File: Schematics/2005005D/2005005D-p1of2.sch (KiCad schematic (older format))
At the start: 2 parts, among them J1 ConnectorB8-100, J2 ConnectorB8-200

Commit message: Finished placing components on drawing 2005005D, and added all of the wiring.  However, there's still a considerable amount of cleanup to be done.
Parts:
- added CR? (x28): Diode, symbol AGC_DSKY:Diode
- added G1: Ground-chassis, symbol AGC_DSKY:Ground-chassis
- added Q? (x56): Transistor-NPN, symbol AGC_DSKY:Transistor-NPN
- added T1, T? (x9): KCORE-PBLKCDGJ, symbol AGC_DSKY:KCORE-PBLKCDGJ
- added T21, T22, T? (x8): KCORE-PBCDKLGJ, symbol AGC_DSKY:KCORE-PBCDKLGJ
- added T23, T24: KCORE-BPCDKLGJ, symbol AGC_DSKY:KCORE-BPCDKLGJ
- added T? (x6): KCORE-BPLKCDGJ, symbol AGC_DSKY:KCORE-BPLKCDGJ
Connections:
- net at J1.110: now also Q?.1 (C), Q?.3 (E), T?.3 (C)
- net at J1.114: now also T?.1 (P)
- net at J1.116: now also T?.8 (J), T?.8 (J)
- net at J1.117: now also CR?.1 (K)
- net at J1.119: now also T?.3 (C)
- net at J1.102: now also Q?.1 (C)
- net at J1.120: now also CR?.1 (K)
- net at J1.121: now also Q?.1 (C), Q?.3 (E), T?.3 (C)
- net at J1.124: now also T?.1 (P)
- net at J1.126: now also T?.8 (J), T?.8 (J)
- net at J1.127: now also CR?.1 (K)
- net at J1.129: now also Q?.1 (C), Q?.3 (E), T?.3 (C)
- net at J1.103: now also T21.1 (P)
- net at J1.130: now also CR?.1 (K)
- net at J1.134: now also T1.1 (P)
- net at J1.136: now also T?.8 (J), T?.8 (J)
- net at J1.137: now also CR?.1 (K)
- net at J1.139: now also Q?.1 (C), Q?.3 (E), T1.3 (C)
- net at J1.104: now also Q?.3 (E), T21.4 (D)
- net at J1.140: now also CR?.1 (K)
- net at J1.141: now also Q?.1 (C), Q?.3 (E), T?.3 (C)
- net at J1.145: now also T?.1 (P)
- net at J1.147: now also T?.8 (J), T?.8 (J)
- net at J1.148: now also CR?.1 (K)
- net at J1.149: now also Q?.3 (E), T?.3 (C)
- net at J1.105: now also T21.8 (J), T22.8 (J), T23.8 (J), T24.8 (J)
- net at J1.150: now also CR?.1 (K)
- net at J1.151: now also Q?.1 (C)
- net at J1.152: now also Q?.1 (C)
- net at J1.153: now also J2.266, Q?.3 (E), Q?.3 (E), Q?.3 (E), Q?.3 (E), Q?.3 (E), Q?.3 (E), Q?.3 (E), Q?.3 (E), T?.5 (K), T?.5 (K), T?.5 (K), T?.5 (K), T?.5 (K), T?.5 (K), T?.5 (K), T?.5 (K)
- net at J1.155: now also T?.1 (P)
- net at J1.156: now also Q?.3 (E), T?.4 (D)
- net at J1.157: now also T?.8 (J), T?.8 (J), T?.8 (J), T?.8 (J)
- net at J1.158: now also CR?.1 (K)
- net at J1.106: now also CR?.1 (K)
- net at J1.160: now also CR?.1 (K)
- net at J1.161: now also Q?.3 (E), T?.4 (D)
- net at J1.163: now also Q?.1 (C)
- net at J1.164: now also T?.1 (P)
- net at J1.165: now also T?.8 (J), T?.8 (J), T?.8 (J), T?.8 (J)
- net at J1.166: now also Q?.3 (E), T?.4 (D)
- net at J1.167: now also CR?.1 (K)
- net at J1.168: now also CR?.1 (K)
- net at J1.169: now also Q?.3 (E), T?.4 (D)
- net at J1.107: now also CR?.1 (K)
- net at J1.108: now also Q?.1 (C), Q?.1 (C), Q?.1 (C), Q?.1 (C), Q?.1 (C), Q?.1 (C), Q?.1 (C), Q?.1 (C), Q?.1 (C), Q?.1 (C), Q?.1 (C), Q?.1 (C)
- net at J1.109: now also Q?.3 (E), T22.4 (D)
- net at J2.201: now also Q?.3 (E), T24.4 (D)
- net at J2.210: now also Q?.1 (C), Q?.3 (E), T?.3 (C)
- net at J2.212: now also CR?.1 (K)
- net at J2.213: now also T?.8 (J), T?.8 (J)
- net at J2.214: now also T?.2 (B)
- net at J2.219: now also Q?.1 (C), Q?.3 (E), T?.3 (C)
- net at J2.202: now also CR?.1 (K)
- net at J2.220: now also CR?.1 (K)
- net at J2.221: now also Q?.1 (C), Q?.3 (E), T?.3 (C)
- net at J2.222: now also CR?.1 (K)
- net at J2.223: now also T?.8 (J), T?.8 (J)
- net at J2.224: now also T?.2 (B)
- net at J2.228: now also Q?.3 (E), Q?.3 (E), Q?.3 (E), Q?.3 (E), Q?.3 (E), Q?.3 (E), Q?.3 (E), Q?.3 (E), T?.6 (L), T?.6 (L), T?.6 (L), T?.6 (L), T?.6 (L), T?.6 (L), T?.6 (L), T?.6 (L)
- net at J2.229: now also Q?.1 (C), Q?.3 (E), T?.3 (C)
- net at J2.203: now also T23.2 (B)
- net at J2.230: now also CR?.1 (K)
- net at J2.231: now also Q?.1 (C), Q?.3 (E), T?.3 (C)
- net at J2.232: now also CR?.1 (K)
- net at J2.233: now also T1.8 (J), T?.8 (J)
- net at J2.234: now also T?.2 (B)
- net at J2.204: now also Q?.3 (E), T23.4 (D)
- net at J2.240: now also Q?.1 (C), Q?.3 (E), T?.3 (C)
- net at J2.241: now also CR?.1 (K)
- net at J2.242: now also Q?.1 (C), Q?.3 (E), T?.3 (C)
- net at J2.243: now also CR?.1 (K)
- net at J2.244: now also T?.8 (J), T?.8 (J)
- net at J2.245: now also T?.2 (B)
- net at J2.248: now also Q?.3 (E), Q?.3 (E), Q?.3 (E), Q?.3 (E), Q?.3 (E), Q?.3 (E), Q?.3 (E), Q?.3 (E), T1.6 (L), T?.6 (L), T?.6 (L), T?.6 (L), T?.6 (L), T?.6 (L), T?.6 (L), T?.6 (L)
- net at J2.249: now also Q?.1 (C), Q?.3 (E), T?.3 (C)
- net at J2.205: now also CR?.1 (K)
- net at J2.250: now also Q?.3 (E), T?.4 (D)
- net at J2.251: now also CR?.1 (K)
- net at J2.252: now also Q?.3 (E), T?.4 (D)
- net at J2.253: now also Q?.1 (C), Q?.1 (C), Q?.1 (C), Q?.1 (C), Q?.1 (C), Q?.1 (C), Q?.1 (C), Q?.1 (C), Q?.1 (C), Q?.1 (C), Q?.1 (C), Q?.1 (C), Q?.1 (C), Q?.1 (C), Q?.1 (C), Q?.3 (E)
- net at J2.254: now also CR?.1 (K)
- net at J2.255: now also T?.2 (B)
- net at J2.258: now also Q?.1 (C)
- net at J2.206: now also Q?.3 (E), Q?.3 (E), Q?.3 (E), T21.5 (K), T22.5 (K), T24.5 (K)
- net at J2.260: now also Q?.1 (C)
- net at J2.261: now also Q?.1 (C), T?.4 (D)
- net at J2.262: now also Q?.3 (E), T?.4 (D)
- net at J2.263: now also CR?.1 (K)
- net at J2.264: now also CR?.1 (K)
- net at J2.265: now also T?.2 (B)
- net at J2.267: now also Q?.1 (C)
- net at J2.268: now also Q?.1 (C)
- net at J2.269: now also G1.1
- net at J2.207: now also Q?.1 (C)
- net at J2.208: now also Q?.1 (C)
- net at J2.209: now also CR?.1 (K)
- new net: T21.2 (B), T22.1 (P)
- new net: T22.2 (B), T24.1 (P)
- new net: Q?.2 (B), T22.3 (C)
- new net: Q?.2 (B), T22.6 (L)
- new net: CR?.2 (A), T22.7 (G)
- new net: T23.1 (P), T24.2 (B)
- new net: Q?.2 (B), T23.3 (C)
- new net: Q?.2 (B), T23.6 (L)
- new net: CR?.2 (A), T23.7 (G)
- new net: Q?.2 (B), T24.3 (C)
- new net: Q?.2 (B), T24.6 (L)
- new net: CR?.2 (A), T24.7 (G)
- new net: Q?.2 (B), T21.3 (C)
- new net: Q?.2 (B), T21.6 (L)
- new net: CR?.2 (A), T21.7 (G)
- new net: T?.1 (P), T?.2 (B) (x17)
- new net: Q?.2 (B), T?.4 (D) (x15)
- new net: Q?.2 (B), T?.5 (K) (x15)
- new net: CR?.2 (A), T?.7 (G) (x23)
- new net: Q?.2 (B), T?.3 (C) (x8)
- new net: Q?.2 (B), T?.6 (L) (x8)
- new net: T1.2 (B), T?.1 (P)
- new net: Q?.2 (B), T1.5 (K)
- new net: CR?.2 (A), T1.7 (G)
- new net: Q?.1 (C), Q?.3 (E) (x2)

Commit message: Completed first draft of transcription of drawing 2005005D.
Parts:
- gave numbers to parts that had none: 107
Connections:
- net at T23.5 (K): now also Q45.3 (E)
- net at J2.261, T28.4 (D): now also Q56.3 (E); no longer Q56.1 (C)
- net at J1.149, Q9.3 (E), T5.3 (C): now also Q10.1 (C)
- net at T2.3 (C): now also J1.131
- net at T1.4 (D): now also Q1.2 (B)
- net at J2.253, Q1.1 (C), Q11.1 (C)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: now also Q56.1 (C); no longer Q56.3 (E)
- net at Q51.1 (C): now also J1.162
- net at Q43.1 (C): now also J1.101
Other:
- note added: "CKT NO. 40201"
- note added: "CKT NO. 40202"
- note added: "CKT NO. 40203"
- note added: "CKT NO. 40204"
- note added: "CKT NO. 40205"
- note added: "CKT NO. 40206"
- note added: "CKT NO. 40207"
- note added: "CKT NO. 40208"
- note added: "CKT NO. 40209"
- note added: "CKT NO. 40210"
- note added: "CKT NO. 40211"
- note added: "CKT NO. 40212"
- note added: "CKT NO. 40213"
- note added: "CKT NO. 40214"
- note added: "CKT NO. 40215"
- note added: "CKT NO. 40216"
- note added: "CKT NO. 40217"
- note added: "CKT NO. 40218"
- note added: "CKT NO. 40219"
- note added: "CKT NO. 40220"
- note added: "CKT NO. 40221"
- note added: "CKT NO. 40222"
- note added: "CKT NO. 40223"
- note added: "CKT NO. 40224"
- note added: "CKT NO. 40225"
- note added: "CKT NO. 40226"
- note added: "CKT NO. 40227"
- note added: "CKT NO. 40228"
- note added: "Notes from the Virtual AGC Project:\n1. This CAD drawing was transcribed from the original Apollo Program drawing\n 2005005D, but does not itself date from the Apollo Program. — RSB 2018\n2. The oval pads numbered 101-169 comprise connector J1, while those \n numbered 201-269 comprise connector J2. — RSB 2018"
- note removed: "Notes from the Virtual AGC Project:\n1. This CAD drawing was transcribed from the original Apollo Program drawing\n 2005005D, but does not itself date from the Apollo Program. — RSB 2018"

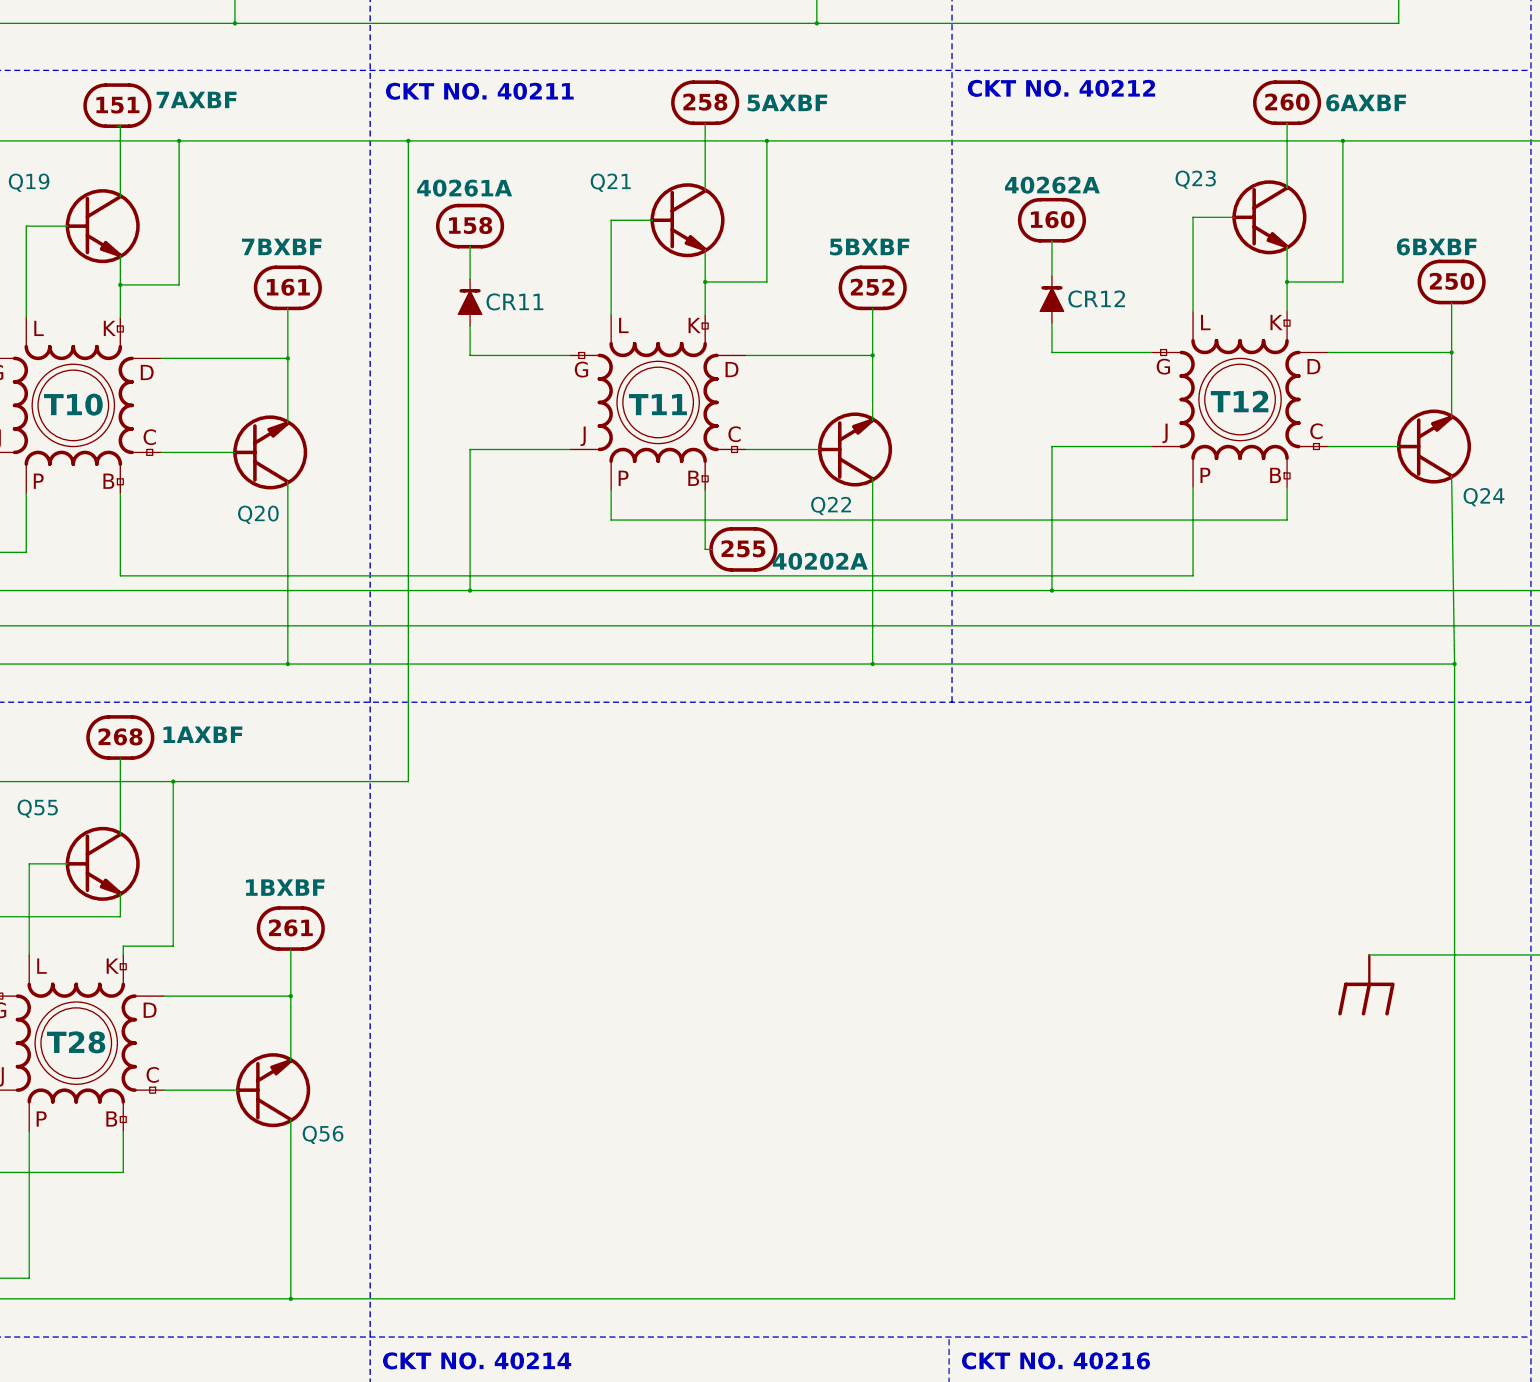
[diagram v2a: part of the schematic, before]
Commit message: Made visual fixes with eelint.  ERC passes.  Netlist was not previously in repo.
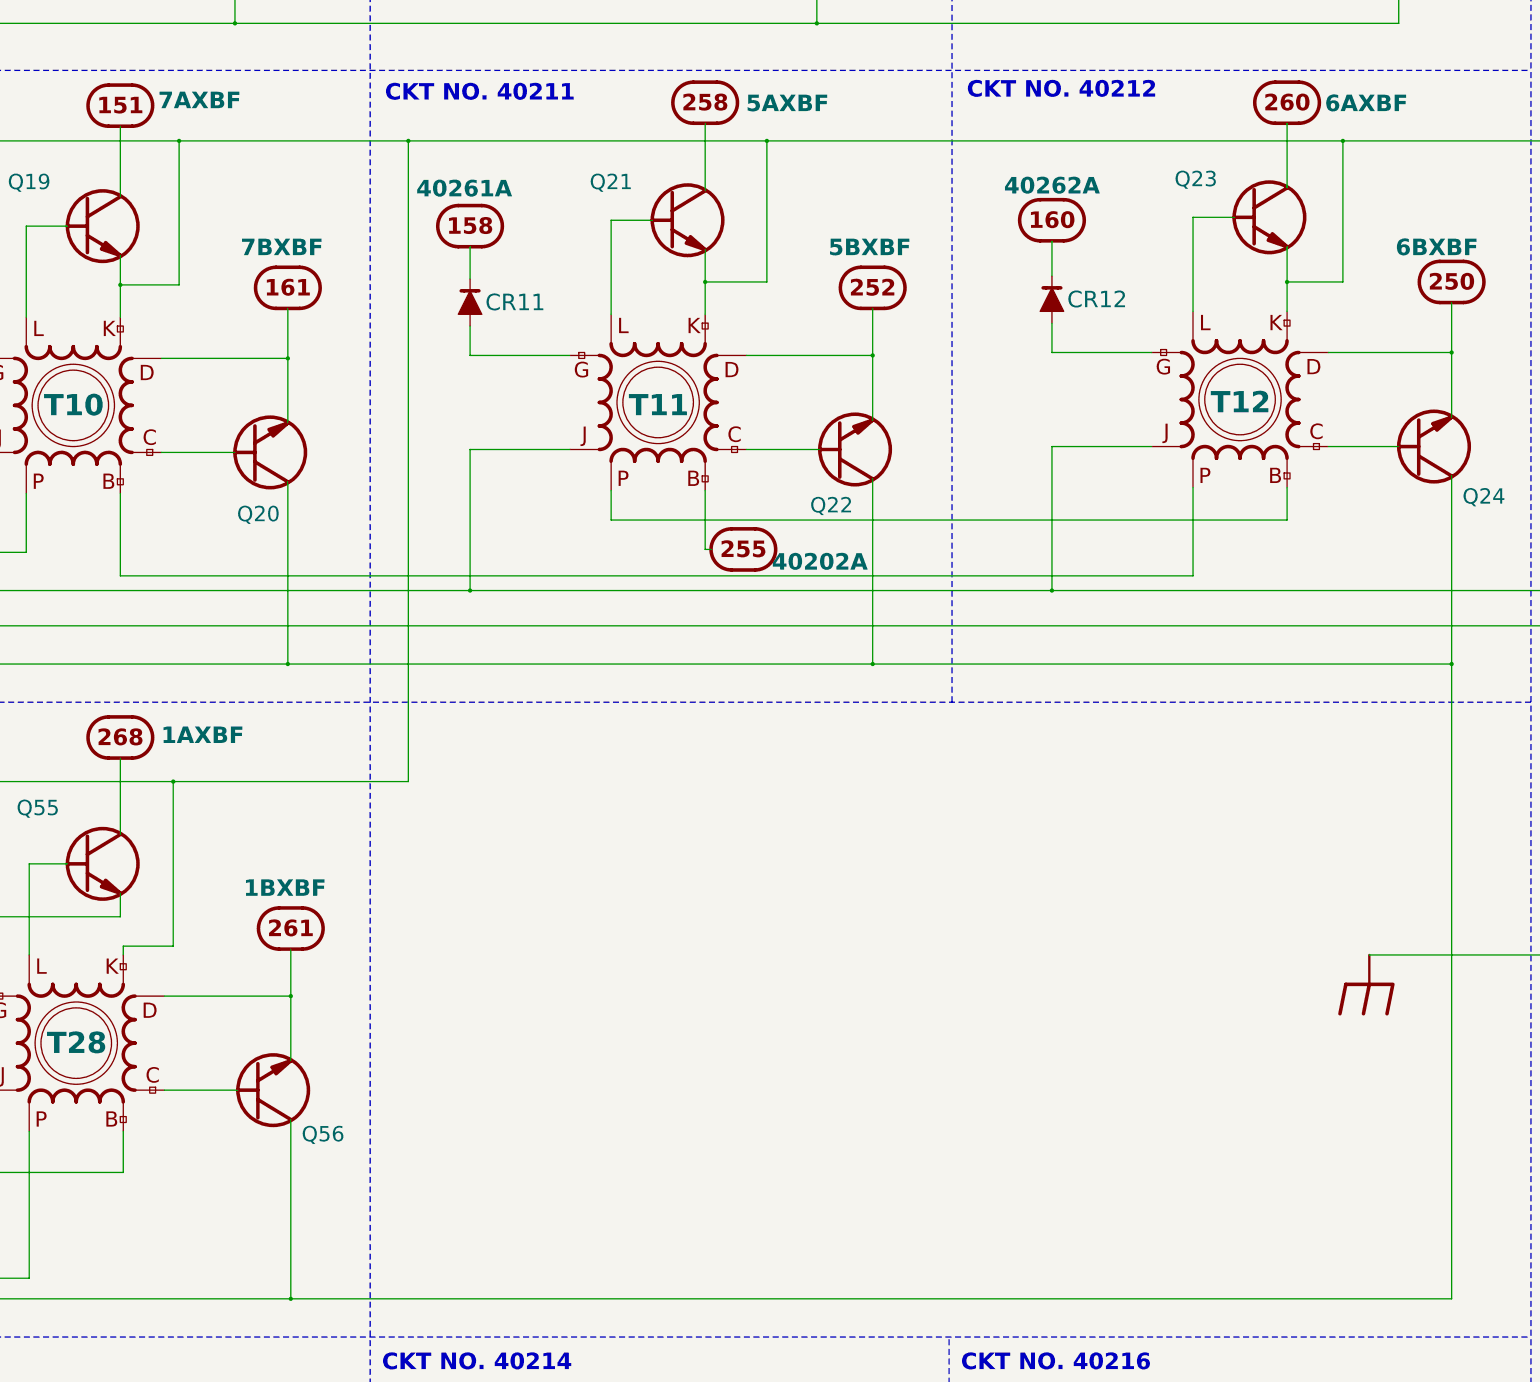
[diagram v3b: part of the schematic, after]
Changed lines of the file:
@@
-EESchema Schematic File Version 4
-LIBS:module-cache
+EESchema Schematic File Version 5
+LIBS:errors-cache
 EELAYER 29 0
 EELAYER END
 $Descr E 44000 34000
 encoding utf-8
-Sheet 2 3
+Sheet 1 1
 Title ""
 Date ""
@@
 L AGC_DSKY:ConnectorB8-100 J1
 U 51 2 5C13955A
-P 21900 7975
-F 0 "J1" H 21900 8300 140 0001 C CNN
-F 1 "ConnectorB8-100" H 21900 8400 140 0001 C CNN
-F 2 "" H 21900 8450 140 0001 C CNN
-F 3 "" H 21900 8450 140 0001 C CNN
-F 4 "7AXBF" H 22575 7850 140 0000 C BNB "Caption"
-	51   21900 7975
+P 21925 7975
+F 0 "J1" H 21925 8300 140 0001 C CNN
+F 1 "ConnectorB8-100" H 21925 8400 140 0001 C CNN
+F 2 "" H 21925 8450 140 0001 C CNN
+F 3 "" H 21925 8450 140 0001 C CNN
+F 4 "7AXBF" H 22600 7850 140 0000 C BNB "Caption"
+	51   21925 7975
 	1    0    0    1
 $EndComp
@@
 	14450 12725 18400 12725
 Wire Wire Line
-	33275 12725 33250 11125
+	33250 12725 33250 11125
 Connection ~ 3675 2850
 Wire Wire Line
 	3675 2850 3175 2850
-Connection ~ 33275 12725
+Connection ~ 33250 12725
 $Comp
 L AGC_DSKY:Ground-chassis G1
@@
 	32550 15200 34825 15200
 Wire Wire Line
-	33275 18125 23375 18125
+	33250 18125 23375 18125
 Wire Wire Line
 	8550 18125 8550 16575
@@
 Connection ~ 28325 12725
 Wire Wire Line
-	28325 12725 33275 12725
+	28325 12725 33250 12725
 Wire Wire Line
 	31050 11225 31050 11975
@@
 	18400 12725 23350 12725
 Wire Wire Line
-	33275 12725 33275 18125
+	33250 12725 33250 18125
 Wire Wire Line
 	23375 16600 23375 18125
@@
 	21925 8750 21925 8150
 Wire Wire Line
-	21925 8150 21900 8150
-Wire Wire Line
 	21925 9775 21925 9500
